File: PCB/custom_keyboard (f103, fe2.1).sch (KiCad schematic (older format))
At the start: 504 parts, among them IC1 FE2.1, J2 Conn_01x04, U1 24LC02BT-I/SN, U10 PRTR5V0U2X, U11 XC6206P332MR, U12 74LVC1G34, U14 MIC2505, U15 MIC2505, U2 PRTR5V0U2X, U3 PRTR5V0U2X, U4 PRTR5V0U2X, U5 PRTR5V0U2X, U6 PRTR5V0U2X, U7 PRTR5V0U2X, U8 SD00HA, U9 STM32F103C8T6, Y1 8MHz, Y3 12MHz

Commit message: Rearranged components on schematic
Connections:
- wire segments 2687 -> 2688
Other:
- note added: "Circuit Breaker"
- note added: "Keyboard Matrix\n"
- note added: "LED Fuse"
- note removed: "Keyboard Matrix"
- note removed: "Matrix"
- moved on the sheet: BOOT0, C1, C10, C11, C12, C13, C14, C16, C17, C18, C19, C2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

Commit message: Tidied up components on schematic and PCB
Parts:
- renumbered IC1 to FE2.1, U9 to STM32
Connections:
- wire segments 2688 -> 2687
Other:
- moved on the sheet: BOOT0, C1, C3, C36, C37, C40, C41, C9, F1, FB15, J2, OL1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

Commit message: Reannotated components
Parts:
- renumbered C48 to C1, C7 to C10, C8 to C11, C34 to C12, C9 to C13, C11 to C14, C12 to C15, C14 to C16, C2 to C17, C4 to C18, C16 to C19, C32 to C2, C17 to C20, C18 to C21, C19 to C22, C20 to C23, C21 to C24, C13 to C25, C24 to C26, C26 to C27, C27 to C28, C28 to C29, C1 to C3, C10 to C30, C29 to C31, C30 to C32, C31 to C33, C44 to C34, C45 to C35, C35 to C38, C38 to C39, C25 to C4, C39 to C40, C46 to C41, C47 to C42, C40 to C43, C41 to C44, C33 to C5, C23 to C6, C3 to C7, C5 to C8, C6 to C9, D9 to D2, D2 to D3, D3 to D4, D4 to D5, D5 to D7, D7 to D8, D8 to D9, F8 to F1, F6 to F2, F5 to F3, F7 to F4, F2 to F5, F4 to F6, F3 to F7, F1 to F8, FB9 to FB1, FB13 to FB10, FB2 to FB11, FB4 to FB12, FB14 to FB13, FB3 to FB14, FB8 to FB2, FB10 to FB3, FB6 to FB4, FB1 to FB5, FB11 to FB6, FB5 to FB7, FB12 to FB8, FB7 to FB9, J2 to J1, R47 to R1, R57 to R10, R33 to R11, R8 to R12, R9 to R13, R28 to R14, R12 to R15, R14 to R16, R40 to R17, R49 to R18, R30 to R19, R58 to R2, R53 to R20, R52 to R21, R5 to R22, R45 to R23, R48 to R24, R39 to R25, R46 to R26, R16 to R27, R60 to R28, R21 to R29, R2 to R3, R59 to R30, R22 to R31, R23 to R32, R10 to R33, R3 to R34, R6 to R35, R11 to R36, R1 to R37, R50 to R38, R51 to R39, R24 to R40, R43 to R41, R25 to R42, R44 to R43, R7 to R44, R61 to R45, R17 to R46, R18 to R47, R62 to R48, R26 to R49, R34 to R5, R35 to R50, R41 to R51, R20 to R52, R19 to R53, R29 to R54, R13 to R55, R36 to R56, R54 to R57, R42 to R58, R32 to R59, R37 to R6, R55 to R60, R15 to R61, R56 to R62, R38 to R63, R27 to R7, R63 to R8, R31 to R9, TP47 to TP10, TP48 to TP11, TP49 to TP12, TP26 to TP13, TP3 to TP14, TP24 to TP15, TP42 to TP16, TP8 to TP17, TP43 to TP18, TP7 to TP20, TP20 to TP21, TP28 to TP22, TP27 to TP23, TP29 to TP24, TP10 to TP25, TP30 to TP26, TP11 to TP27, TP31 to TP28, TP50 to TP29, TP21 to TP3, TP12 to TP30, TP32 to TP31, TP51 to TP32, TP37 to TP33, TP33 to TP34, TP38 to TP35, TP18 to TP36, TP13 to TP37, TP16 to TP38, TP52 to TP39, TP22 to TP4, TP14 to TP40, TP17 to TP41, TP34 to TP42, TP36 to TP43, TP35 to TP44, TP39 to TP45, TP5 to TP46, TP40 to TP47, TP6 to TP48, TP41 to TP49, TP23 to TP5, TP15 to TP50, TP9 to TP51, TP53 to TP52, TP54 to TP53, TP25 to TP6, TP44 to TP7, TP45 to TP8, TP46 to TP9, U8 to U1, U4 to U10, U15 to U11, U11 to U12, U12 to U13, U7 to U3, U6 to U4, U1 to U5, U10 to U6, U3 to U7, U5 to U8, U14 to U9, Y3 to Y1, Y1 to Y2

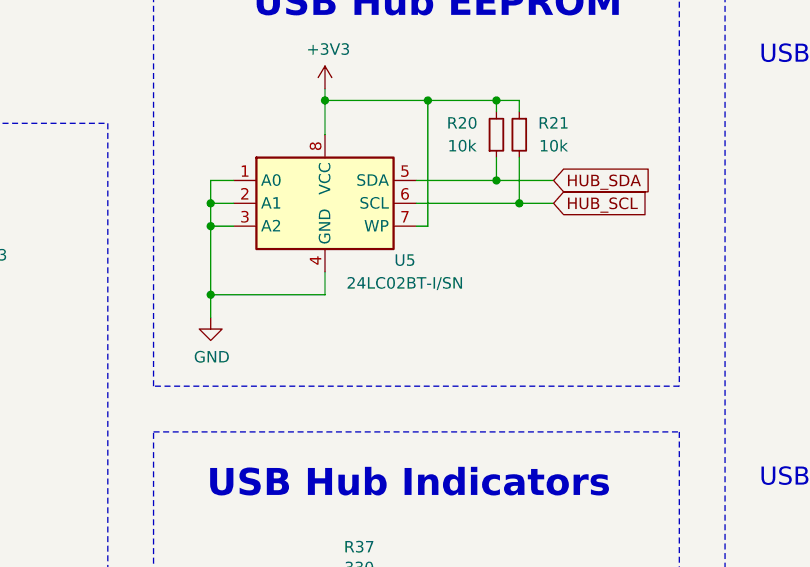
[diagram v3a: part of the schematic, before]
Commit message: Added logo, copyright, and credits
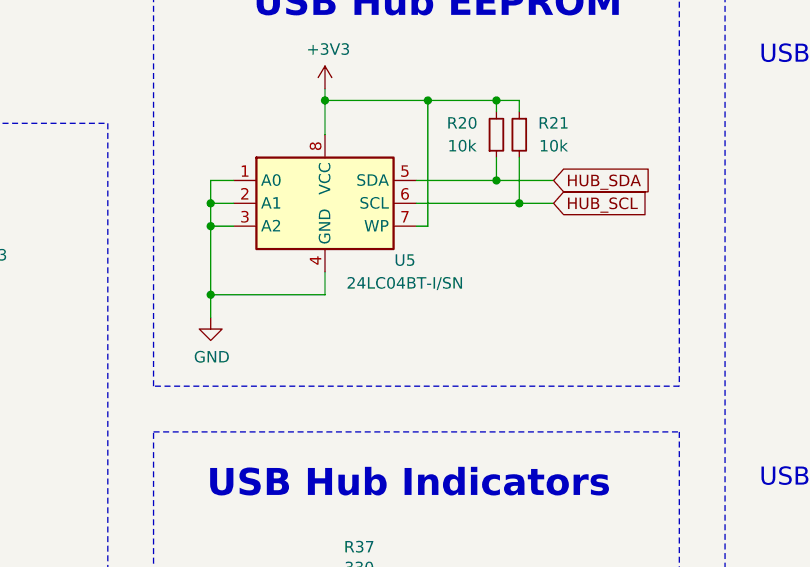
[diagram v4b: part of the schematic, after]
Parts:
- U5: value 24LC02BT-I/SN -> 24LC04BT-I/SN
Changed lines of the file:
@@
 P 19400 14350
 F 0 "U5" H 19750 14100 50  0000 C CNN
-F 1 "24LC02BT-I/SN" H 19750 14000 50  0000 C CNN
+F 1 "24LC04BT-I/SN" H 19750 14000 50  0000 C CNN
 F 2 "custom-footprints:24LC04" H 19400 14350 50  0001 C CNN
 F 3 "http://ww1.microchip.com/downloads/en/DeviceDoc/21709c.pdf" H 19400 14350 50  0001 C CNN

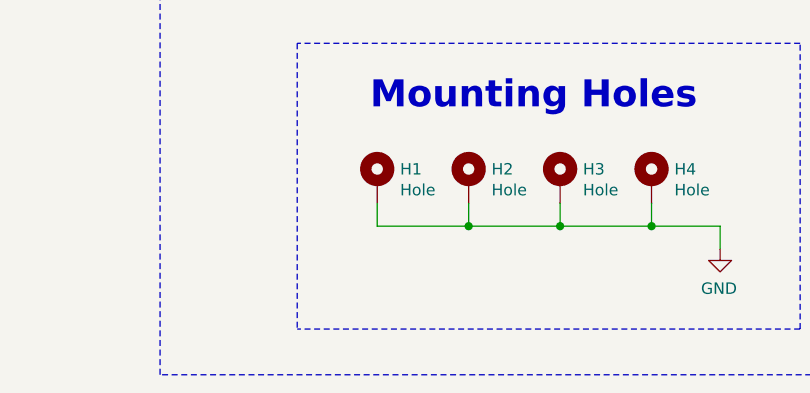
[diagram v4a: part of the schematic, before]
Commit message: Moved resistors closer to usb hub ic
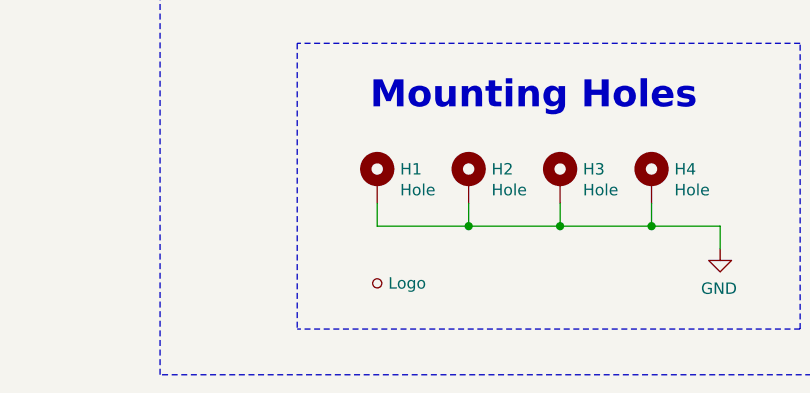
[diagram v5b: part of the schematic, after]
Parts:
- added TP54: Logo, custom-footprints:logo, symbol Connector:TestPoint_Small
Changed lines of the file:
@@
 	27050 17850 27700 17850
 Wire Wire Line
-	27700 17950 27850 17950
-Wire Wire Line
 	27850 18250 27850 17950
 Connection ~ 27850 17950
@@
 	22300 16250 23400 16250
 Wire Wire Line
-	23400 16250 23550 16250
-Wire Wire Line
 	23550 16650 23550 16250
 Connection ~ 23550 16250
@@
 	22300 14400 23400 14400
 Wire Wire Line
-	23850 14400 23950 14400
-Wire Wire Line
-	23400 14400 23550 14400
-Wire Wire Line
-	23850 14500 23950 14500
-Wire Wire Line
 	22750 14500 23400 14500
 Wire Wire Line
-	23400 14500 23650 14500
-Wire Wire Line
 	23550 14800 23550 14400
 Connection ~ 23550 14400
@@
 	22300 12550 23400 12550
 Wire Wire Line
-	23850 12550 23950 12550
-Wire Wire Line
-	23400 12550 23550 12550
-Wire Wire Line
 	22750 12650 23400 12650
 Wire Wire Line
-	23850 12650 23950 12650
-Wire Wire Line
-	23400 12650 23650 12650
-Wire Wire Line
 	23550 12950 23550 12550
 Connection ~ 23550 12550
@@
 	23550 16250 23650 16250
 Wire Wire Line
-	23850 16250 23950 16250
-Wire Wire Line
-	23850 16350 23950 16350
-Wire Wire Line
-	23400 16350 23650 16350
-Wire Wire Line
-	27700 17850 27950 17850
-Wire Wire Line
-	28150 17850 28350 17850
-Wire Wire Line
-	28150 17950 28350 17950
-Wire Wire Line
 	27850 17950 27950 17950
 Text GLabel 28350 15350 2    50   Input ~ 0
@@
 	27050 15350 27700 15350
 Wire Wire Line
-	27700 15450 27850 15450
-Wire Wire Line
 	27850 15750 27850 15450
 Connection ~ 27850 15450
 Wire Wire Line
-	27700 15350 27950 15350
-Wire Wire Line
-	28150 15350 28350 15350
-Wire Wire Line
-	28150 15450 28350 15450
-Wire Wire Line
 	27850 15450 27950 15450
 $Comp
@@
 Wire Wire Line
 	27850 13000 27950 13000
-Wire Wire Line
-	28150 13000 28350 13000
-Wire Wire Line
-	28150 12900 28350 12900
-Wire Wire Line
-	27700 12900 27950 12900
 Connection ~ 27850 13000
 Wire Wire Line
-	27700 13000 27850 13000
-Wire Wire Line
 	27850 13300 27850 13000
 Wire Wire Line
@@
 Wire Wire Line
 	21600 15000 21600 15150
+Wire Wire Line
+	28150 15450 28350 15450
+Wire Wire Line
+	27700 15450 27850 15450
+Wire Wire Line
+	28150 15350 28350 15350
+Wire Wire Line
+	27700 15350 27950 15350
+Wire Wire Line
+	28150 17950 28350 17950
+Wire Wire Line
+	27700 17950 27850 17950
+Wire Wire Line
+	28150 17850 28350 17850
+Wire Wire Line
+	27700 17850 27950 17850
+Wire Wire Line
+	23850 16350 23950 16350
+Wire Wire Line
+	23400 16350 23650 16350
+Wire Wire Line
+	23850 16250 23950 16250
+Wire Wire Line
+	23400 16250 23550 16250
+Wire Wire Line
+	28150 13000 28350 13000
+Wire Wire Line
+	27700 13000 27850 13000
+Wire Wire Line
+	28150 12900 28350 12900
+Wire Wire Line
+	27700 12900 27950 12900
+Wire Wire Line
+	23850 12650 23950 12650
+Wire Wire Line
+	23400 12650 23650 12650
+Wire Wire Line
+	23850 12550 23950 12550
+Wire Wire Line
+	23400 12550 23550 12550
+Wire Wire Line
+	23400 14500 23650 14500
+Wire Wire Line
+	23850 14500 23950 14500
+Wire Wire Line
+	23850 14400 23950 14400
+Wire Wire Line
+	23400 14400 23550 14400
+$Comp
+L Connector:TestPoint_Small TP54
+U 1 1 823B3101
+P 4700 20900
+F 0 "TP54" H 4748 20946 50  0001 L CNN
+F 1 "Logo" H 4748 20900 50  0000 L CNN
+F 2 "custom-footprints:logo" H 4900 20900 50  0001 C CNN
+F 3 "~" H 4900 20900 50  0001 C CNN
+	1    4700 20900
+	1    0    0    -1
+$EndComp
 $EndSCHEMATC

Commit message: Added indicator LEDs to keyboard power
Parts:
- added D11, D12: Red, LED_SMD:LED_0805_2012Metric, symbol Device:LED_Small
- added R64, R65: 330, Resistor_SMD:R_0805_2012Metric, symbol Device:R_Small
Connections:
- wire segments 2687 -> 2695
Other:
- moved on the sheet: FB2, FB5

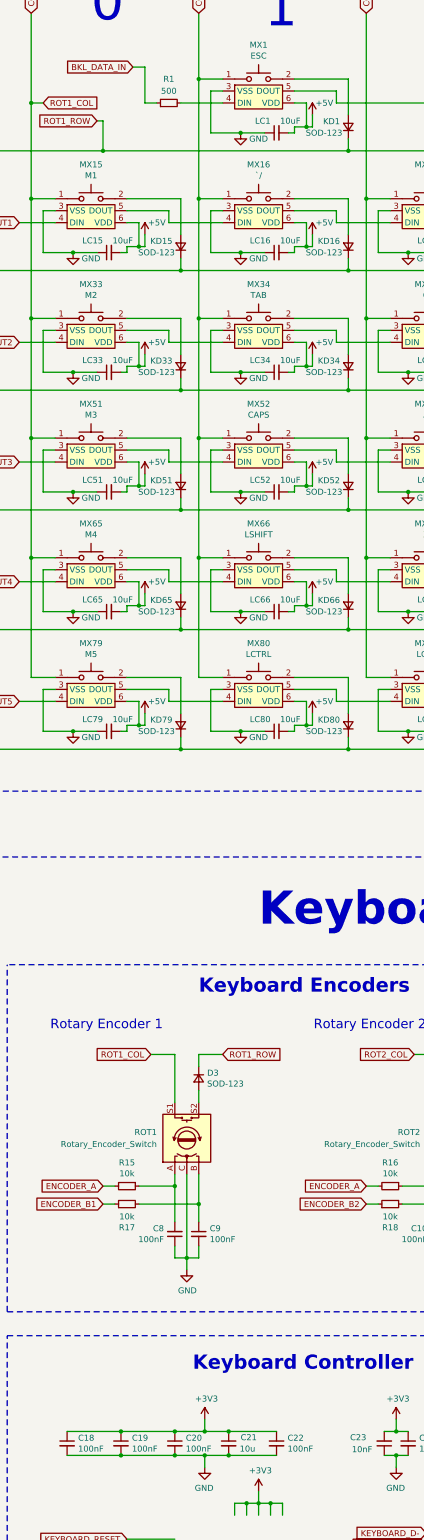
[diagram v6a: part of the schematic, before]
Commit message: Added guard traces, double checked part numbers
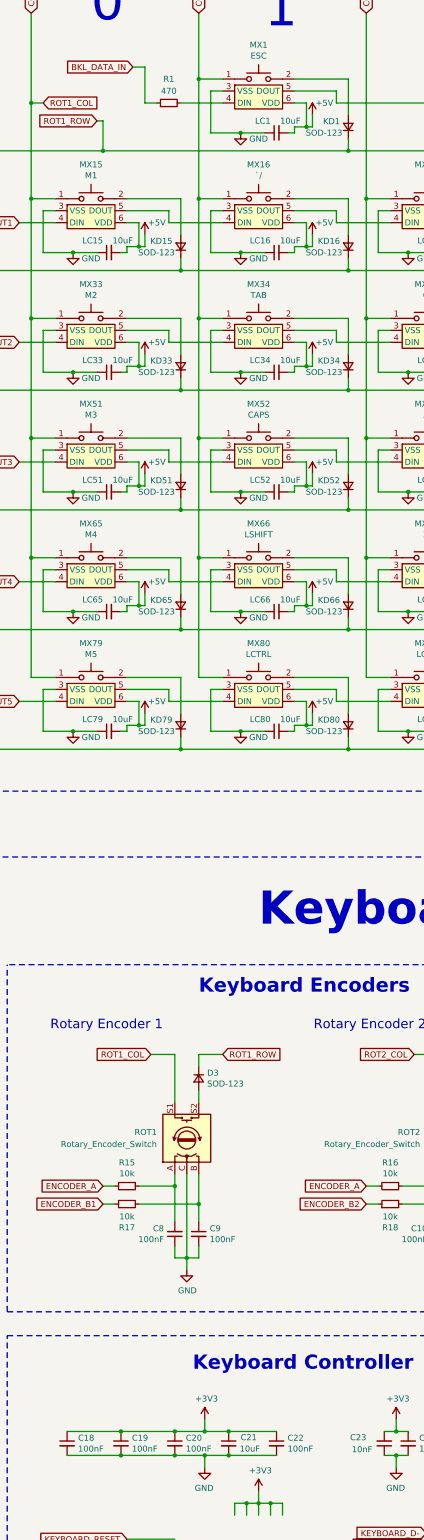
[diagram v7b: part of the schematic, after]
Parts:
- C21: value 10u -> 10uF; LCSC Part C1779 -> C15850
- C34, C41: LCSC Part C15850 -> C49678
- R1: value 500 -> 470
- R14, R33, R36, R50, R56, R7: LCSC Part C27834 -> C17756
- R19: LCSC Part C17414 -> C17513
- R27: footprint Resistor_SMD:R_0603_1608Metric -> Resistor_SMD:R_0805_2012Metric; LCSC Part C25803 -> C17414
- TP54: JLCPCB BOM (none) -> 0
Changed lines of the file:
@@
 F 2 "Capacitor_SMD:C_0805_2012Metric" H 22500 18750 50  0001 C CNN
 F 3 "~" H 22500 18750 50  0001 C CNN
-F 4 "C15850" H 22500 18750 50  0001 C CNN "LCSC Part"
+F 4 "C49678" H 22500 18750 50  0001 C CNN "LCSC Part"
 	1    22500 18750
 	1    0    0    -1
@@
 F 2 "Capacitor_SMD:C_0805_2012Metric" H 22500 19500 50  0001 C CNN
 F 3 "~" H 22500 19500 50  0001 C CNN
-F 4 "C15850" H 22500 19500 50  0001 C CNN "LCSC Part"
+F 4 "C49678" H 22500 19500 50  0001 C CNN "LCSC Part"
 	1    22500 19500
 	1    0    0    -1
@@
 	23550 12950 23550 12550
 Connection ~ 23550 12550
-Wire Wire Line
-	23550 12550 23650 12550
 $Comp
 L Device:R_Small R41
@@
 $EndComp
 Wire Wire Line
-	23550 16250 23650 16250
-Wire Wire Line
 	27850 17950 27950 17950
 Text GLabel 28350 15350 2    50   Input ~ 0
@@
 F 2 "Resistor_SMD:R_0805_2012Metric" H 26650 15150 50  0001 C CNN
 F 3 "~" H 26650 15150 50  0001 C CNN
-F 4 "C27834" H 26650 15150 50  0001 C CNN "LCSC Part"
+F 4 "C17756" H 26650 15150 50  0001 C CNN "LCSC Part"
 	1    26650 15150
 	1    0    0    -1
@@
 F 2 "Resistor_SMD:R_0805_2012Metric" H 26550 15650 50  0001 C CNN
 F 3 "~" H 26550 15650 50  0001 C CNN
-F 4 "C27834" H 26550 15650 50  0001 C CNN "LCSC Part"
+F 4 "C17756" H 26550 15650 50  0001 C CNN "LCSC Part"
 	1    26550 15650
 	1    0    0    -1
@@
 F 2 "Resistor_SMD:R_0805_2012Metric" H 26650 12700 50  0001 C CNN
 F 3 "~" H 26650 12700 50  0001 C CNN
-F 4 "C27834" H 26650 12700 50  0001 C CNN "LCSC Part"
+F 4 "C17756" H 26650 12700 50  0001 C CNN "LCSC Part"
 	1    26650 12700
 	1    0    0    -1
@@
 F 2 "Resistor_SMD:R_0805_2012Metric" H 26550 13200 50  0001 C CNN
 F 3 "~" H 26550 13200 50  0001 C CNN
-F 4 "C27834" H 26550 13200 50  0001 C CNN "LCSC Part"
+F 4 "C17756" H 26550 13200 50  0001 C CNN "LCSC Part"
 	1    26550 13200
 	1    0    0    -1
@@
 F 2 "Resistor_SMD:R_0805_2012Metric" H 26650 17650 50  0001 C CNN
 F 3 "~" H 26650 17650 50  0001 C CNN
-F 4 "C27834" H 26650 17650 50  0001 C CNN "LCSC Part"
+F 4 "C17756" H 26650 17650 50  0001 C CNN "LCSC Part"
 	1    26650 17650
 	1    0    0    -1
@@
 F 2 "Resistor_SMD:R_0805_2012Metric" H 26550 18150 50  0001 C CNN
 F 3 "~" H 26550 18150 50  0001 C CNN
-F 4 "C27834" H 26550 18150 50  0001 C CNN "LCSC Part"
+F 4 "C17756" H 26550 18150 50  0001 C CNN "LCSC Part"
 	1    26550 18150
 	1    0    0    -1
@@
 P 5800 15550
 F 0 "C21" H 5900 15600 50  0000 L CNN
-F 1 "10u" H 5892 15505 50  0000 L CNN
+F 1 "10uF" H 5892 15505 50  0000 L CNN
 F 2 "Capacitor_SMD:C_0805_2012Metric" H 5800 15550 50  0001 C CNN
 F 3 "~" H 5800 15550 50  0001 C CNN
-F 4 "C1779" H 5800 15550 50  0001 C CNN "LCSC Part"
+F 4 "C15850" H 5800 15550 50  0001 C CNN "LCSC Part"
 	1    5800 15550
 	1    0    0    -1
@@
 F 2 "Resistor_SMD:R_0805_2012Metric" H 10800 14050 50  0001 C CNN
 F 3 "~" H 10800 14050 50  0001 C CNN
-F 4 "C17414" H 10800 14050 50  0001 C CNN "LCSC Part"
+F 4 "C17513" H 10800 14050 50  0001 C CNN "LCSC Part"
 	1    10800 14050
 	1    0    0    -1
@@
 F 0 "R27" V 10304 14700 50  0000 C CNN
 F 1 "10k" V 10395 14700 50  0000 C CNN
-F 2 "Resistor_SMD:R_0603_1608Metric" H 10500 14700 50  0001 C CNN
+F 2 "Resistor_SMD:R_0805_2012Metric" H 10500 14700 50  0001 C CNN
 F 3 "~" H 10500 14700 50  0001 C CNN
-F 4 "C25803" H 10500 14700 50  0001 C CNN "LCSC Part"
+F 4 "C17414" H 10500 14700 50  0001 C CNN "LCSC Part"
 	1    10500 14700
 	0    -1   1    0
@@
 P 5300 4350
 F 0 "R1" V 5500 4350 50  0000 C CNN
-F 1 "500" V 5400 4350 50  0000 C CNN
+F 1 "470" V 5400 4350 50  0000 C CNN
 F 2 "Resistor_SMD:R_0805_2012Metric" H 5300 4350 50  0001 C CNN
 F 3 "~" H 5300 4350 50  0001 C CNN
@@
 	27700 15350 27950 15350
 Wire Wire Line
-	28150 17950 28350 17950
-Wire Wire Line
-	27700 17950 27850 17950
-Wire Wire Line
-	28150 17850 28350 17850
-Wire Wire Line
-	27700 17850 27950 17850
-Wire Wire Line
-	23850 16350 23950 16350
-Wire Wire Line
-	23400 16350 23650 16350
-Wire Wire Line
-	23850 16250 23950 16250
-Wire Wire Line
 	23400 16250 23550 16250
 Wire Wire Line
@@
 	27700 12900 27950 12900
 Wire Wire Line
-	23850 12650 23950 12650
-Wire Wire Line
-	23400 12650 23650 12650
-Wire Wire Line
-	23850 12550 23950 12550
-Wire Wire Line
 	23400 12550 23550 12550
 Wire Wire Line
@@
 F 2 "custom-footprints:logo" H 4900 20900 50  0001 C CNN
 F 3 "~" H 4900 20900 50  0001 C CNN
+F 4 "0" H 4700 20900 50  0001 C CNN "JLCPCB BOM"
 	1    4700 20900
 	1    0    0    -1
@@
 	18100 12200 18250 12200
 Connection ~ 18250 12200
+Wire Wire Line
+	28150 17950 28350 17950
+Wire Wire Line
+	27700 17950 27850 17950
+Wire Wire Line
+	27700 17850 27950 17850
+Wire Wire Line
+	28150 17850 28350 17850
+Wire Wire Line
+	23400 12650 23650 12650
+Wire Wire Line
+	23850 12650 23950 12650
+Wire Wire Line
+	23850 12550 23950 12550
+Wire Wire Line
+	23550 12550 23650 12550
+Wire Wire Line
+	23400 16350 23650 16350
+Wire Wire Line
+	23850 16350 23950 16350
+Wire Wire Line
+	23850 16250 23950 16250
+Wire Wire Line
+	23550 16250 23650 16250
 $EndSCHEMATC
